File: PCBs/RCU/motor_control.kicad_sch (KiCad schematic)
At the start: 40 parts, among them J300 Right_Encoder_Conn, J301 Right_Motor_Screw_Terminal, U300 OPA365xxD, U301 DRV8876, U302 OPA365xxD, U303 DRV8876

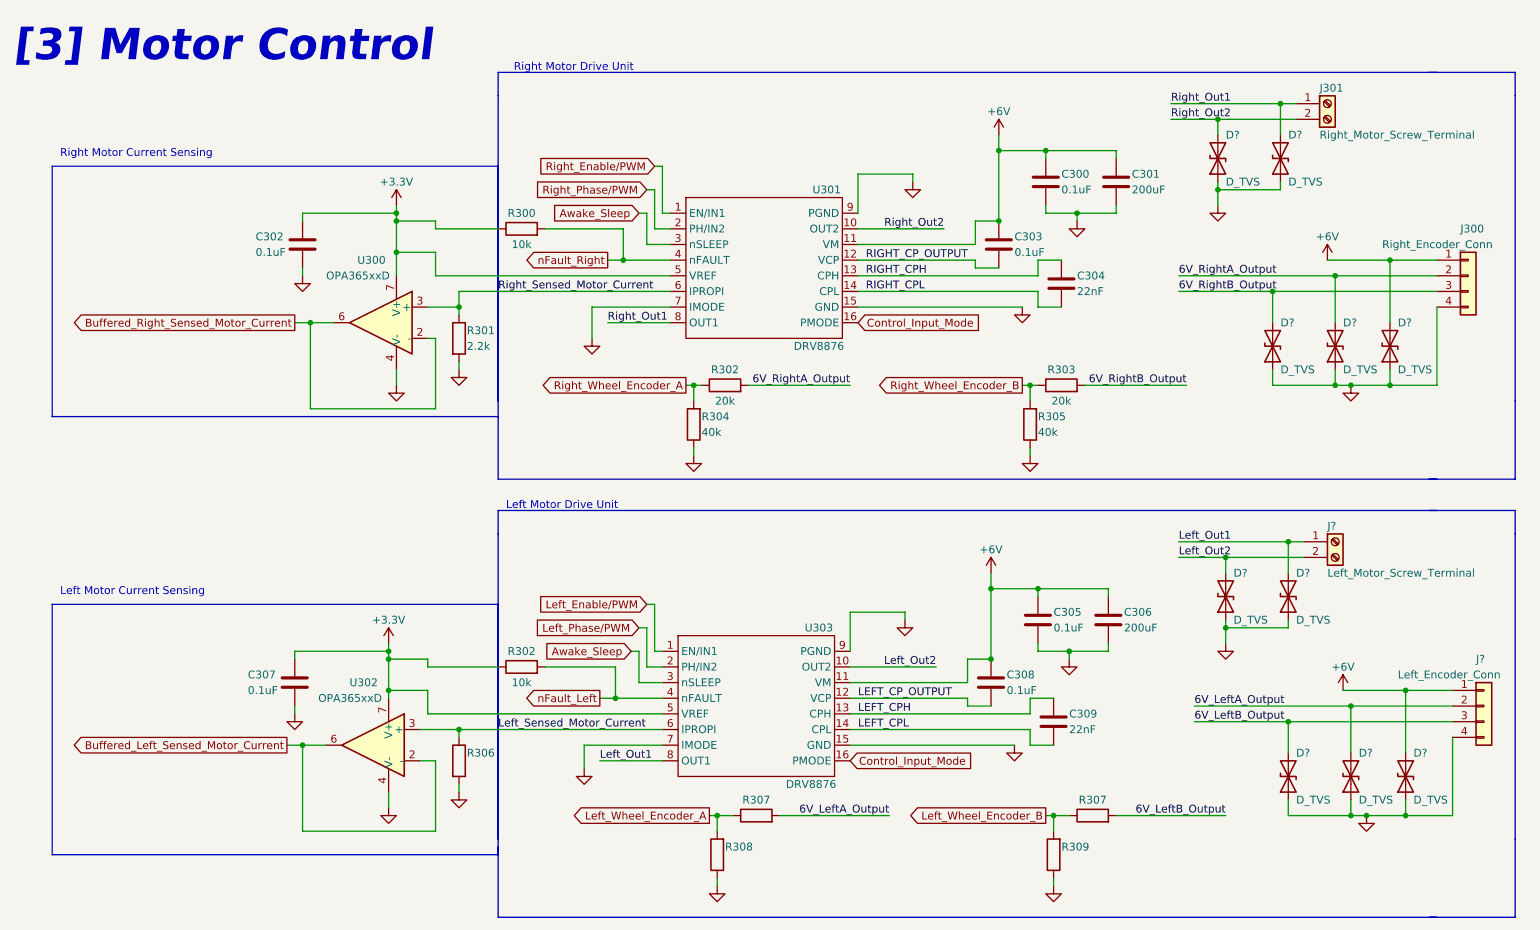
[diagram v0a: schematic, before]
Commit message: Removed TVS diodes for motor terminals, label TVS diodes for encoder, using OPA320 op amps in motor control schematic, it is now fully annotated
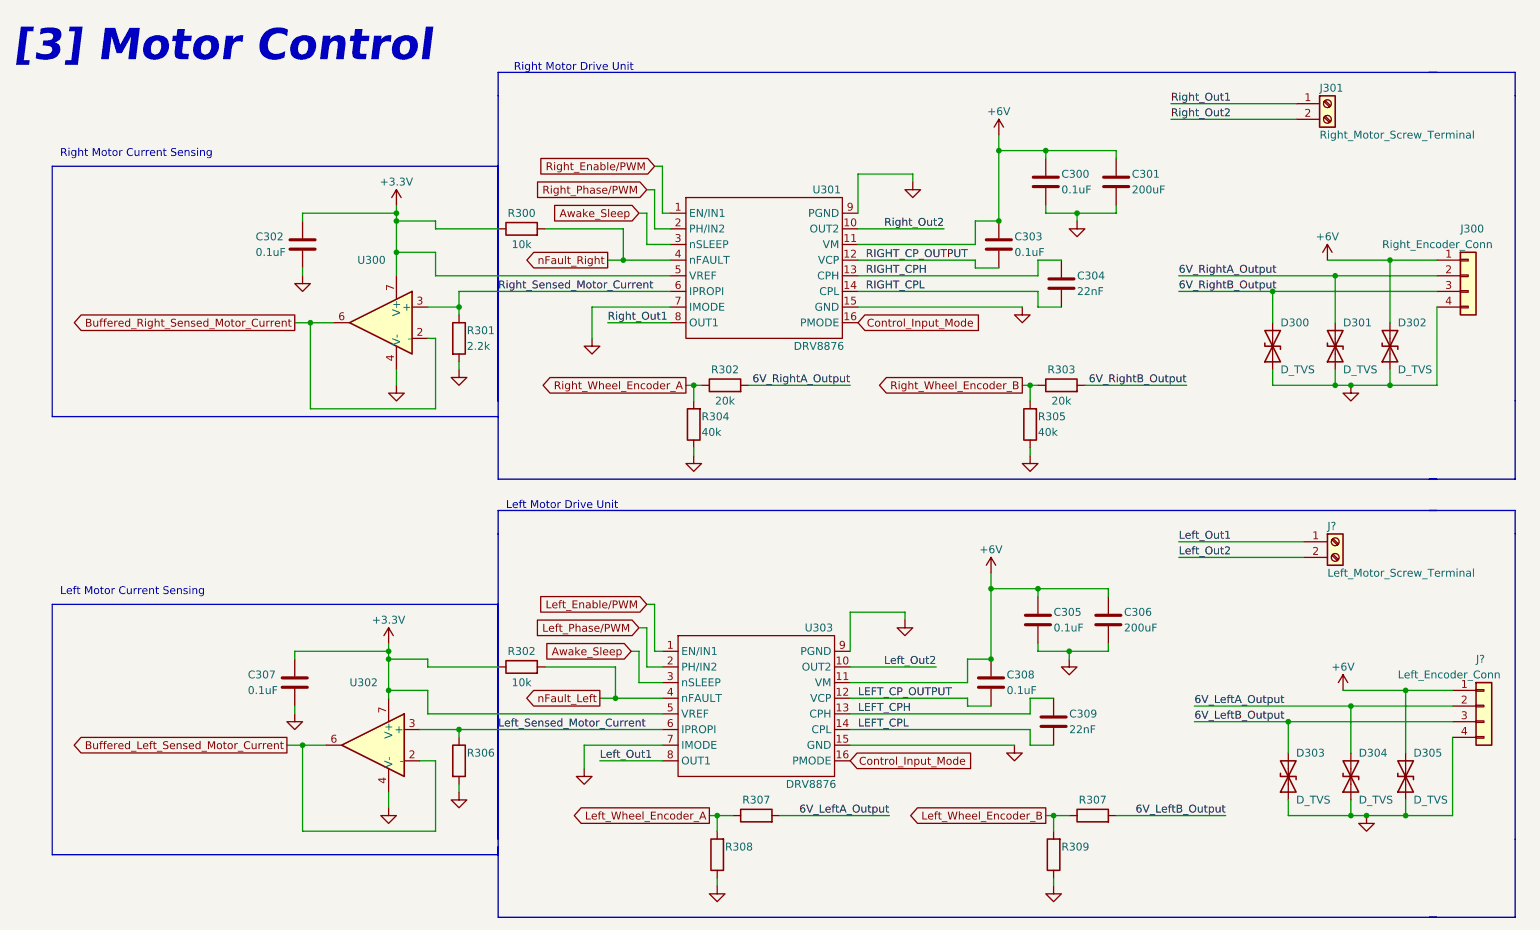
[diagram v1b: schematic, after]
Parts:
- removed D? (x4): D_TVS, symbol Device:D_TVS
- U300, U302: value OPA365xxD -> (none)
- gave numbers to parts that had none: 6

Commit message: Labled motor terminala and encoder connectors
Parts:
- gave numbers to parts that had none: 2
- renumbered J301 to J300, J300 to J301
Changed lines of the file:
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@@
   (symbol (lib_id "Connector:Screw_Terminal_01x02") (at 238.76 101.6 0) (unit 1)
     (in_bom yes) (on_board yes)
-    (property "Reference" "J?" (id 0) (at 237.49 99.06 0)
+    (property "Reference" "J302" (id 0) (at 237.49 99.06 0)
       (effects (font (size 1.27 1.27)) (justify left))
     )
@@
   (symbol (lib_id "Connector:Screw_Terminal_01x02") (at 237.49 30.48 0) (unit 1)
     (in_bom yes) (on_board yes)
-    (property "Reference" "J301" (id 0) (at 236.22 27.94 0)
+    (property "Reference" "J300" (id 0) (at 236.22 27.94 0)
       (effects (font (size 1.27 1.27)) (justify left))
     )
@@
   (symbol (lib_id "Connector_Generic:Conn_01x04") (at 262.89 128.27 0) (unit 1)
     (in_bom yes) (on_board yes)
-    (property "Reference" "J?" (id 0) (at 261.62 120.65 0)
+    (property "Reference" "J303" (id 0) (at 261.62 120.65 0)
       (effects (font (size 1.27 1.27)) (justify left))
     )
@@
   (symbol (lib_id "Connector_Generic:Conn_01x04") (at 260.35 58.42 0) (unit 1)
     (in_bom yes) (on_board yes)
-    (property "Reference" "J300" (id 0) (at 259.08 50.8 0)
-      (effects (font (size 1.27 1.27)) (justify left))
-    )
+    (property "Reference" "J301" (id 0) (at 259.08 50.8 0)
+      (effects (font (size 1.27 1.27)) (justify left))
+    )

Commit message: Corrected SPI_MOSI and SPI_MISO labels on U700 - external memory
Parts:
- R306: value (none) -> 2.2k
- R307: value (none) -> 20k
- R308, R309: value (none) -> 40k
- U300, U302: value (none) -> OPA320xxD
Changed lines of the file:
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@@
       (effects (font (size 1.27 1.27)) (justify left))
     )
-    (property "Value" "" (id 1) (at 97.79 138.43 0)
+    (property "Value" "2.2k" (id 1) (at 97.79 138.43 0)
       (effects (font (size 1.27 1.27)) (justify left))
     )
@@
     (in_bom yes) (on_board yes)
     (property "Reference" "R307" (id 0) (at 199.39 143.51 90))
-    (property "Value" "" (id 1) (at 199.39 148.59 90))
+    (property "Value" "20k" (id 1) (at 199.39 148.59 90))
     (property "Footprint" "" (id 2) (at 199.39 147.828 90)
       (effects (font (size 1.27 1.27)) hide)
@@
       (effects (font (size 1.27 1.27)) (justify right))
     )
-    (property "Value" "" (id 1) (at 194.31 153.67 0)
+    (property "Value" "40k" (id 1) (at 194.31 153.67 0)
       (effects (font (size 1.27 1.27)) (justify right))
     )
@@
       (effects (font (size 1.27 1.27)) (justify right))
     )
-    (property "Value" "" (id 1) (at 139.7 153.67 0)
+    (property "Value" "40k" (id 1) (at 139.7 153.67 0)
       (effects (font (size 1.27 1.27)) (justify right))
     )
@@
       (effects (font (size 1.27 1.27)) (justify right))
     )
-    (property "Value" "" (id 1) (at 74.93 58.42 0)
+    (property "Value" "OPA320xxD" (id 1) (at 74.93 58.42 0)
       (effects (font (size 1.27 1.27)) (justify right))
     )
@@
     (in_bom yes) (on_board yes)
     (property "Reference" "R307" (id 0) (at 144.78 143.51 90))
-    (property "Value" "" (id 1) (at 144.78 148.59 90))
+    (property "Value" "20k" (id 1) (at 144.78 148.59 90))
     (property "Footprint" "" (id 2) (at 144.78 147.828 90)
       (effects (font (size 1.27 1.27)) hide)
@@
       (effects (font (size 1.27 1.27)) (justify right))
     )
-    (property "Value" "" (id 1) (at 73.66 127 0)
-      (effects (font (size 1.27 1.27)) (justify right))
-    )
+    (property "Value" "OPA320xxD" (id 1) (at 73.66 127 0)
+      (effects (font (size 1.27 1.27)) (justify right))
+    )

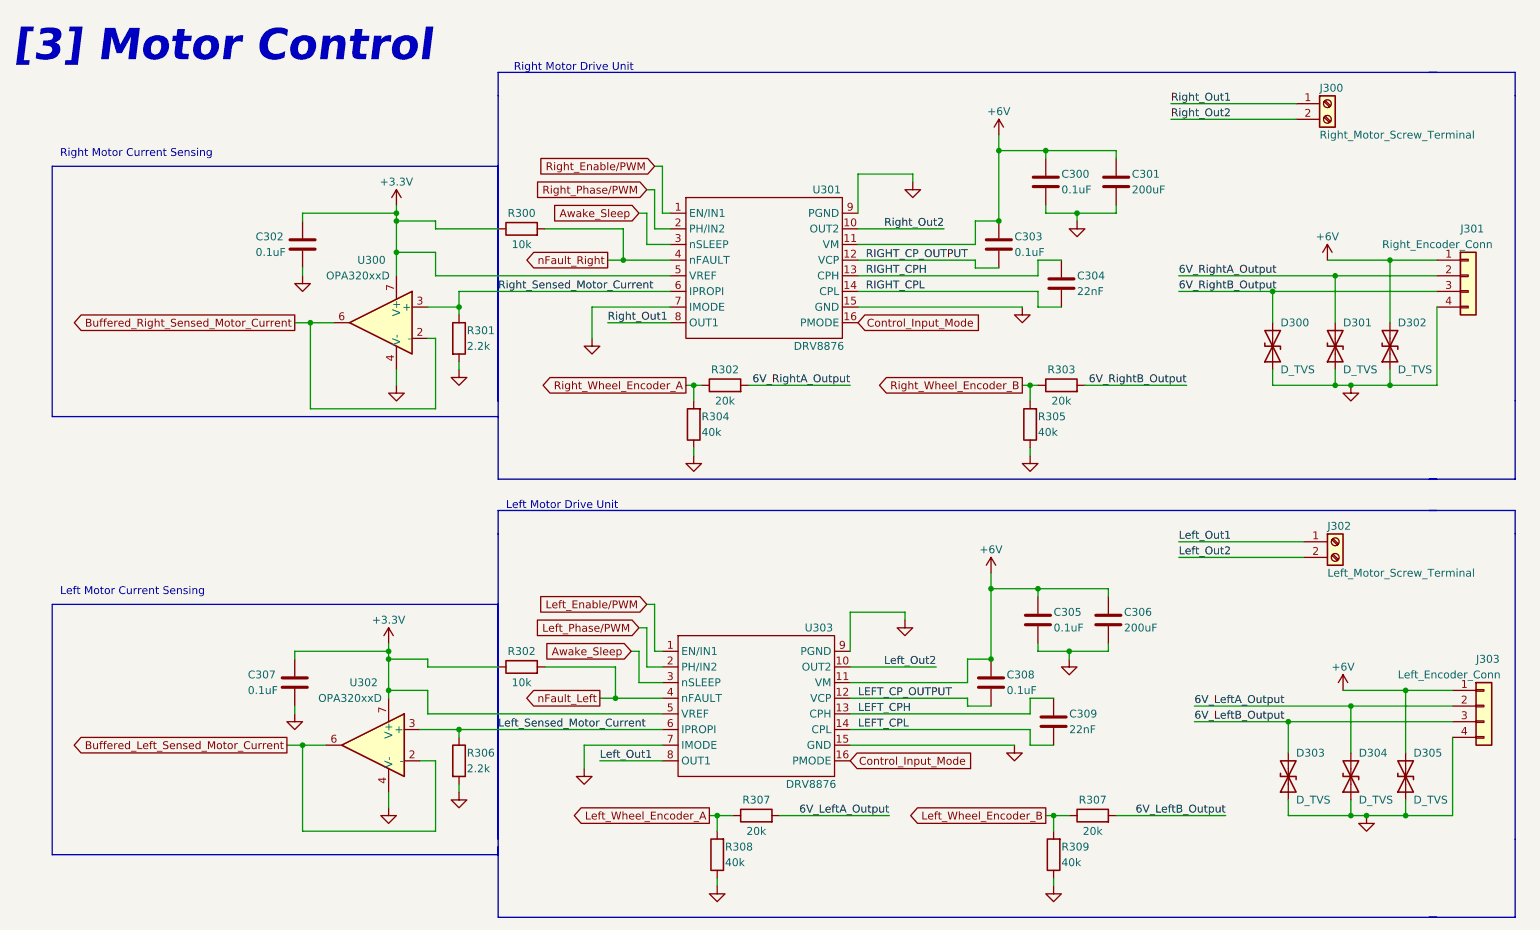
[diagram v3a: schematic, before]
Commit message: Add OPA320, DRV8876, Motor Terminal and encoder footprints
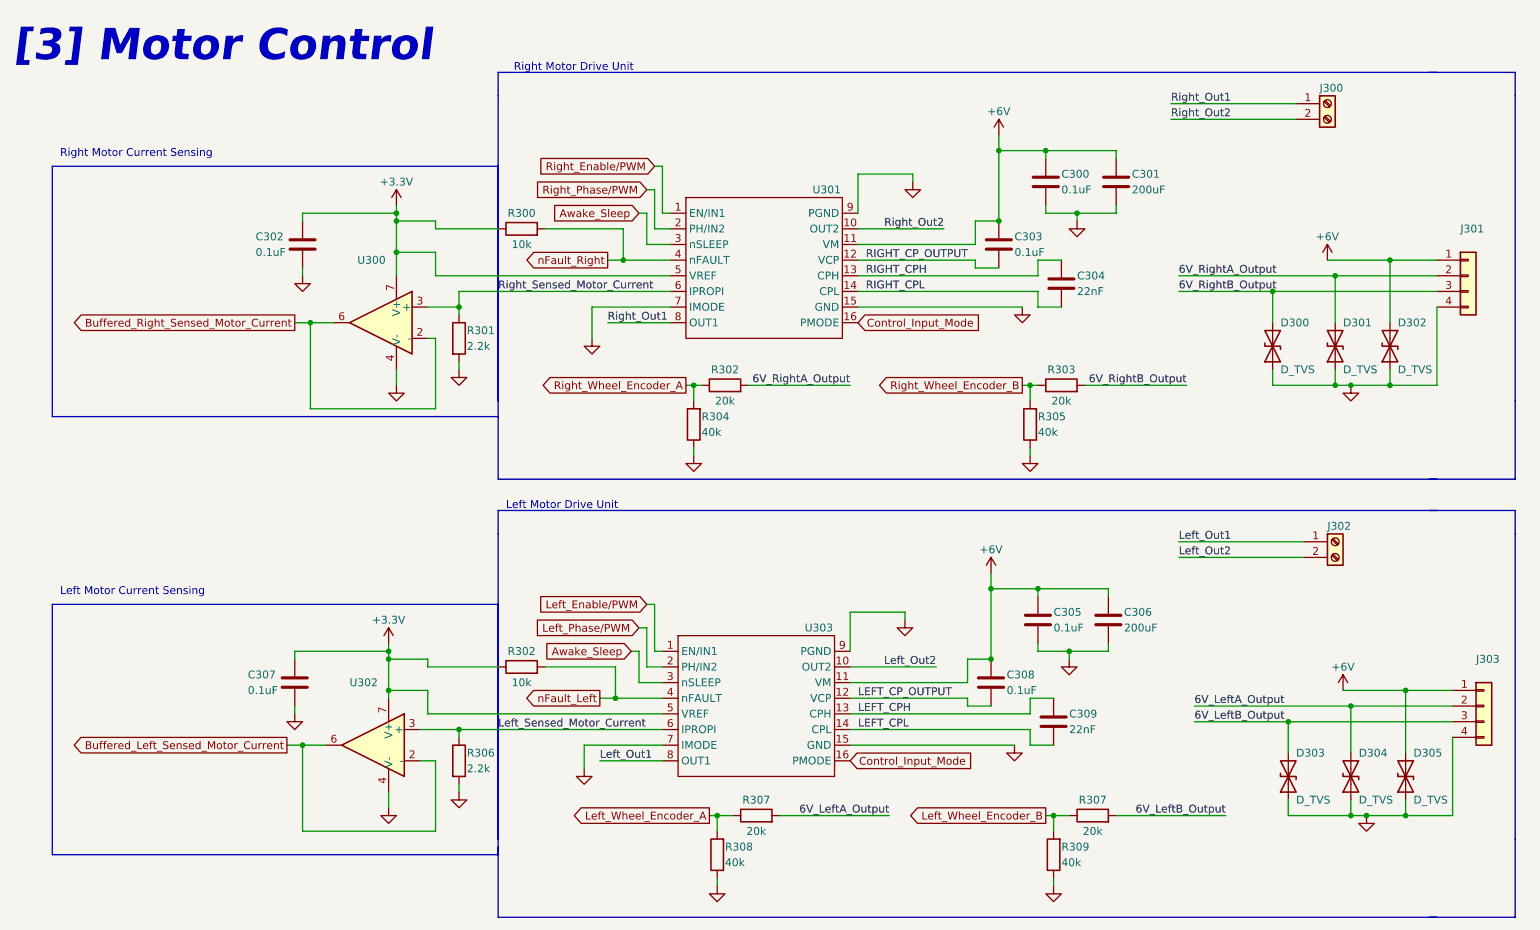
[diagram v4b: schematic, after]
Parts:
- J300: value Right_Motor_Screw_Terminal -> (none)
- J301: value Right_Encoder_Conn -> (none)
- J302: value Left_Motor_Screw_Terminal -> (none)
- J303: value Left_Encoder_Conn -> (none)
- U300, U302: value OPA320xxD -> (none); footprint Package_SO:SOIC-8_3.9x4.9mm_P1.27mm -> (none)
- U301, U303: value DRV8876 -> (none)
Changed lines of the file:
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@@
     (in_bom yes) (on_board yes)
     (property "Reference" "U301" (id 0) (at 156.21 44.45 0))
-    (property "Value" "DRV8876" (id 1) (at 154.94 69.85 0))
+    (property "Value" "" (id 1) (at 154.94 69.85 0))
     (property "Footprint" "" (id 2) (at 146.05 55.88 0)
       (effects (font (size 1.27 1.27)) hide)
@@
       (effects (font (size 1.27 1.27)) (justify left))
     )
-    (property "Value" "Left_Motor_Screw_Terminal" (id 1) (at 237.49 106.68 0)
+    (property "Value" "" (id 1) (at 237.49 106.68 0)
       (effects (font (size 1.27 1.27)) (justify left))
     )
@@
       (effects (font (size 1.27 1.27)) (justify left))
     )
-    (property "Value" "Right_Motor_Screw_Terminal" (id 1) (at 236.22 35.56 0)
+    (property "Value" "" (id 1) (at 236.22 35.56 0)
       (effects (font (size 1.27 1.27)) (justify left))
     )
@@
       (effects (font (size 1.27 1.27)) (justify left))
     )
-    (property "Value" "Left_Encoder_Conn" (id 1) (at 248.92 123.19 0)
+    (property "Value" "" (id 1) (at 248.92 123.19 0)
       (effects (font (size 1.27 1.27)) (justify left))
     )
@@
       (effects (font (size 1.27 1.27)) (justify left))
     )
-    (property "Value" "Right_Encoder_Conn" (id 1) (at 246.38 53.34 0)
+    (property "Value" "" (id 1) (at 246.38 53.34 0)
       (effects (font (size 1.27 1.27)) (justify left))
     )
@@
       (effects (font (size 1.27 1.27)) (justify right))
     )
-    (property "Value" "OPA320xxD" (id 1) (at 74.93 58.42 0)
-      (effects (font (size 1.27 1.27)) (justify right))
-    )
-    (property "Footprint" "Package_SO:SOIC-8_3.9x4.9mm_P1.27mm" (id 2) (at 86.36 71.12 0)
+    (property "Value" "" (id 1) (at 74.93 58.42 0)
+      (effects (font (size 1.27 1.27)) (justify right))
+    )
+    (property "Footprint" "" (id 2) (at 86.36 71.12 0)
       (effects (font (size 1.27 1.27)) (justify left) hide)
     )
-    (property "Datasheet" "http://www.ti.com/lit/ds/symlink/opa365.pdf" (id 3) (at 80.01 62.23 0)
+    (property "Datasheet" "" (id 3) (at 80.01 62.23 0)
       (effects (font (size 1.27 1.27)) hide)
     )
@@
     (in_bom yes) (on_board yes)
     (property "Reference" "U303" (id 0) (at 154.94 115.57 0))
-    (property "Value" "DRV8876" (id 1) (at 153.67 140.97 0))
+    (property "Value" "" (id 1) (at 153.67 140.97 0))
     (property "Footprint" "" (id 2) (at 144.78 127 0)
       (effects (font (size 1.27 1.27)) hide)
@@
       (effects (font (size 1.27 1.27)) (justify right))
     )
-    (property "Value" "OPA320xxD" (id 1) (at 73.66 127 0)
-      (effects (font (size 1.27 1.27)) (justify right))
-    )
-    (property "Footprint" "Package_SO:SOIC-8_3.9x4.9mm_P1.27mm" (id 2) (at 85.09 139.7 0)
+    (property "Value" "" (id 1) (at 73.66 127 0)
+      (effects (font (size 1.27 1.27)) (justify right))
+    )
+    (property "Footprint" "" (id 2) (at 85.09 139.7 0)
       (effects (font (size 1.27 1.27)) (justify left) hide)
     )
-    (property "Datasheet" "http://www.ti.com/lit/ds/symlink/opa365.pdf" (id 3) (at 78.74 130.81 0)
-      (effects (font (size 1.27 1.27)) hide)
-    )
+    (property "Datasheet" "" (id 3) (at 78.74 130.81 0)
+      (effects (font (size 1.27 1.27)) hide)
+    )
